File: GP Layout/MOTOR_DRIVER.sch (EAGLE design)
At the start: 34 parts, among them U2 CSD18502KCS_KCS_3, U3 MIC4604YM, U4 CSD18502KCS_KCS_3, U5 CSD18502KCS_KCS_3, U6 MIC4604YM, U7 ATMEGA328P_TQFP, Y1 16MHz

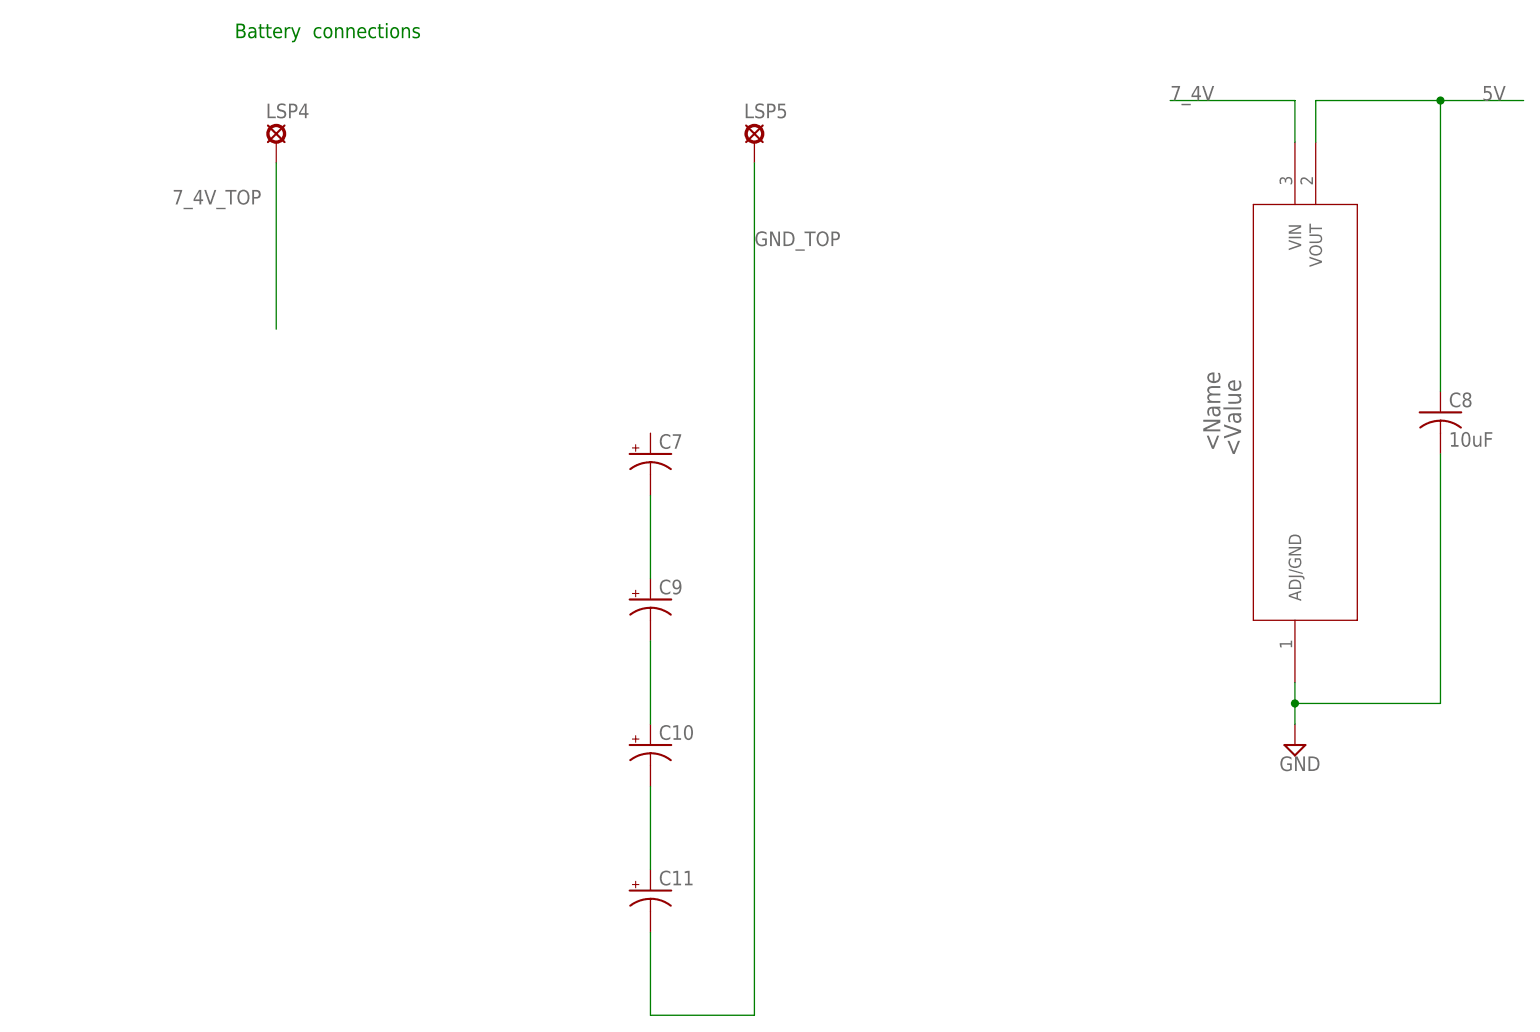
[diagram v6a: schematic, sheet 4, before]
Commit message: modified power schematic, added battery sense, named motor terminals
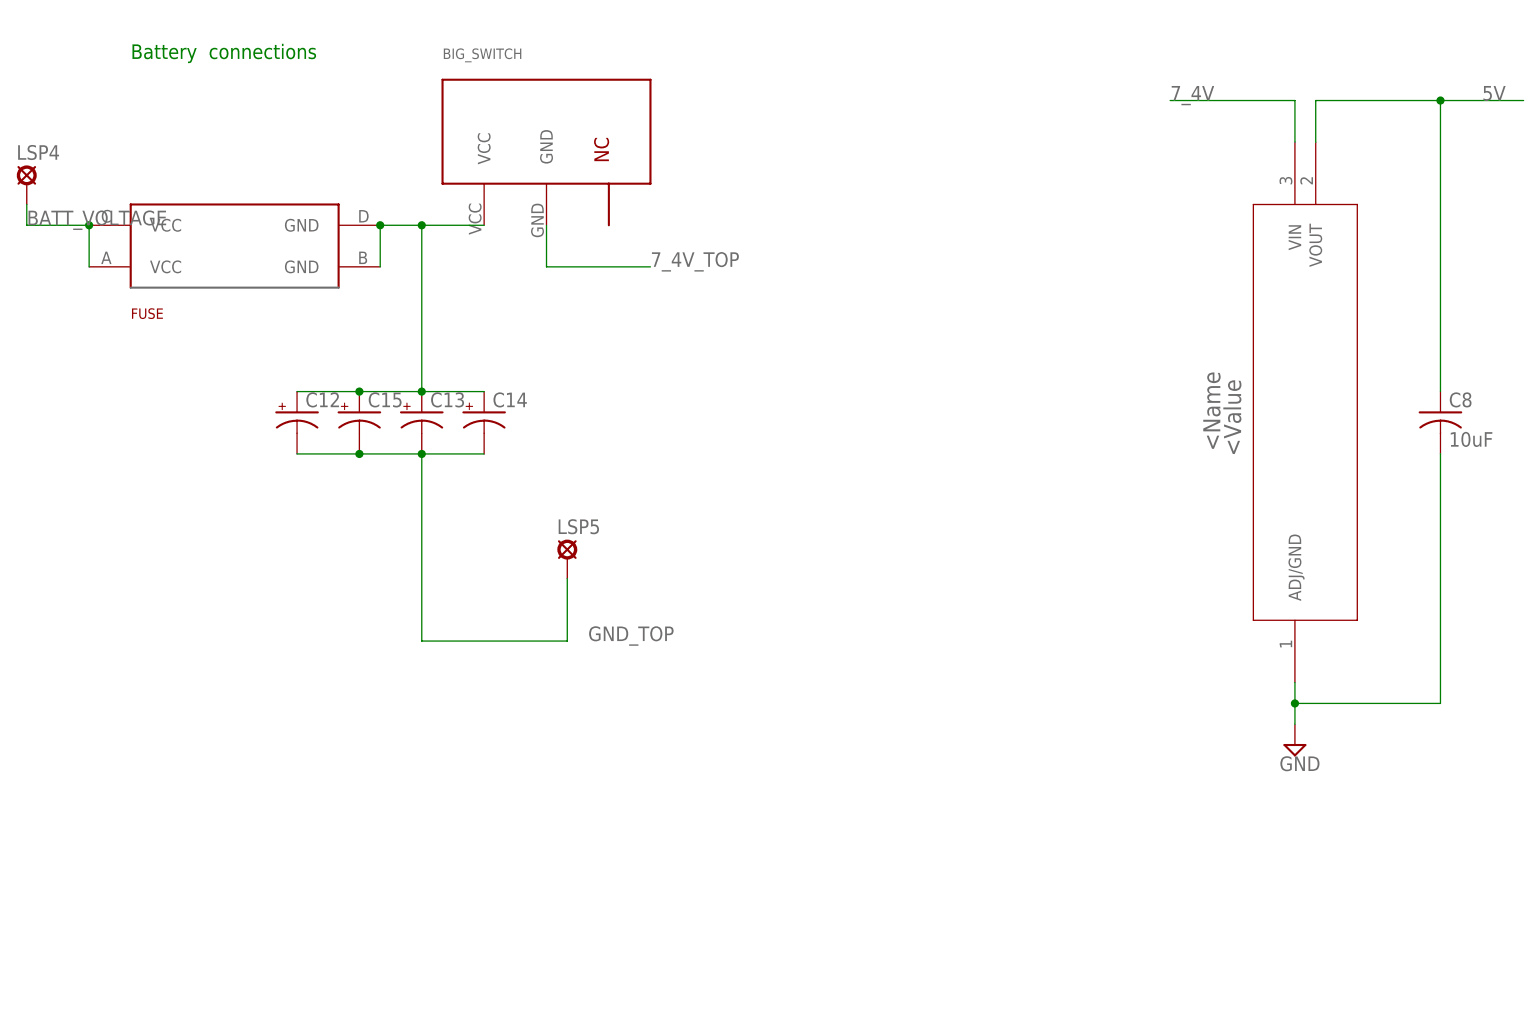
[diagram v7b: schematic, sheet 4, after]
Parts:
- removed C10, C11, C7, C9: (no value), resistor:CPOL-US153CLV-1010
- added BIG_SWITCH: (no value), bigswitch:BIGSWITCH
- added C12, C13, C14, C15: (no value), resistor:CPOL-US153CLV-1010
- added FUSE: (no value), minifuse:FUSEHOLDER3588
- added R1: 2.8M, SparkFun-Resistors:0.3OHM-0805-1/8W-1%
- added R2: 1.62M, SparkFun-Resistors:0.3OHM-0805-1/8W-1%
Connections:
- net N$1 renamed MOTOR_HIGH
- net N$8 renamed MOTOR_LOW
- removed net N$14: C10.-, C11.+
- removed net N$17: C10.+, C9.-
- removed net N$19: C7.-, C9.+
- new net BATT_VOLTAGE: FUSE.VCC@A, FUSE.VCC@C, LSP4.MP, R1.2
- new net BATT_VOLTAGE_SENSE: R1.1, R2.2, U$1.14/A0
- new net N$21: BIG_SWITCH.VCC, C12.+, C13.+, C14.+, C15.+, FUSE.GND@B, FUSE.GND@D
- net 7_4V_TOP: now also BIG_SWITCH.GND; no longer LSP4.MP
- net GND: now also R2.1
- net GND_TOP: now also C12.-, C13.-, C14.-, C15.-; no longer C11.-
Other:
- moved on the sheet: LSP4, LSP5
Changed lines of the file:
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@@
 <?xml version="1.0" encoding="utf-8"?>
 <!DOCTYPE eagle SYSTEM "eagle.dtd">
-<eagle version="8.0.0">
+<eagle version="8.0.1">
 <drawing>
 <settings>
@@
 <part name="SUPPLY1" library="supply2" deviceset="GND" device=""/>
 <part name="C8" library="resistor" deviceset="C-US" device="050-025X075" value="10uF"/>
-<part name="C7" library="resistor" deviceset="CPOL-US" device="153CLV-1010"/>
-<part name="C9" library="resistor" deviceset="CPOL-US" device="153CLV-1010"/>
-<part name="C10" library="resistor" deviceset="CPOL-US" device="153CLV-1010"/>
-<part name="C11" library="resistor" deviceset="CPOL-US" device="153CLV-1010"/>
+<part name="C12" library="resistor" deviceset="CPOL-US" device="153CLV-1010"/>
+<part name="C13" library="resistor" deviceset="CPOL-US" device="153CLV-1010"/>
+<part name="C14" library="resistor" deviceset="CPOL-US" device="153CLV-1010"/>
+<part name="C15" library="resistor" deviceset="CPOL-US" device="153CLV-1010"/>
+<part name="FUSE" library="minifuse" deviceset="FUSEHOLDER3588" device=""/>
+<part name="BIG_SWITCH" library="bigswitch" deviceset="BIGSWITCH" device=""/>
+<part name="R1" library="SparkFun-Resistors" deviceset="0.3OHM" device="-0805-1/8W-1%" value="2.8M"/>
+<part name="R2" library="SparkFun-Resistors" deviceset="0.3OHM" device="-0805-1/8W-1%" value="1.62M"/>
+<part name="SUPPLY2" library="supply2" deviceset="GND" device=""/>
 </parts>
 <sheets>
@@
 </busses>
 <nets>
-<net name="N$1" class="0">
+<net name="MOTOR_HIGH" class="0">
 <segment>
 <pinref part="TOP_FWD" gate="A" pin="SOURCE"/>
@@
 <wire x1="139.7" y1="132.08" x2="127" y2="132.08" width="0.1524" layer="91"/>
 <junction x="127" y="132.08"/>
+<label x="127" y="134.62" size="1.778" layer="95"/>
 </segment>
 </net>
@@
 </segment>
 </net>
-<net name="N$8" class="0">
+<net name="MOTOR_LOW" class="0">
 <segment>
 <pinref part="U4" gate="A" pin="SOURCE"/>
@@
 <wire x1="228.6" y1="132.08" x2="241.3" y2="132.08" width="0.1524" layer="91"/>
 <junction x="241.3" y="132.08"/>
+<label x="228.6" y="134.62" size="1.778" layer="95"/>
 </segment>
 </net>
@@
 <instance part="SUPPLY5" gate="GND" x="320.04" y="154.94"/>
 <instance part="SUPPLY6" gate="GND" x="317.5" y="121.92"/>
+<instance part="R1" gate="G$1" x="342.9" y="144.78" rot="R90"/>
+<instance part="R2" gate="G$1" x="342.9" y="129.54" rot="R90"/>
+<instance part="SUPPLY2" gate="GND" x="342.9" y="119.38"/>
 </instances>
 <busses>
@@
 <pinref part="SUPPLY6" gate="GND" pin="GND"/>
 </segment>
+<segment>
+<pinref part="R2" gate="G$1" pin="1"/>
+<pinref part="SUPPLY2" gate="GND" pin="GND"/>
+<wire x1="342.9" y1="124.46" x2="342.9" y2="121.92" width="0.1524" layer="91"/>
+</segment>
 </net>
 <net name="N$6" class="0">
@@
 <wire x1="289.56" y1="167.64" x2="279.4" y2="167.64" width="0.1524" layer="91"/>
 <label x="284.48" y="167.64" size="1.778" layer="95"/>
+</segment>
+</net>
+<net name="BATT_VOLTAGE_SENSE" class="0">
+<segment>
+<pinref part="U$1" gate="G$1" pin="14/A0"/>
+<wire x1="279.4" y1="137.16" x2="342.9" y2="137.16" width="0.1524" layer="91"/>
+<pinref part="R1" gate="G$1" pin="1"/>
+<wire x1="342.9" y1="137.16" x2="342.9" y2="139.7" width="0.1524" layer="91"/>
+<pinref part="R2" gate="G$1" pin="2"/>
+<wire x1="342.9" y1="134.62" x2="342.9" y2="137.16" width="0.1524" layer="91"/>
+<junction x="342.9" y="137.16"/>
+<label x="312.42" y="137.16" size="1.778" layer="95"/>
+</segment>
+</net>
+<net name="BATT_VOLTAGE" class="0">
+<segment>
+<pinref part="R1" gate="G$1" pin="2"/>
+<wire x1="342.9" y1="149.86" x2="342.9" y2="157.48" width="0.1524" layer="91"/>
+<label x="342.9" y="157.48" size="1.778" layer="95"/>
 </segment>
 </net>
@@
 <description>Power Schematic</description>
 <plain>
-<text x="38.1" y="243.84" size="1.778" layer="91">Battery  connections</text>
+<text x="25.4" y="241.3" size="1.778" layer="91">Battery  connections</text>
 </plain>
 <instances>
 <instance part="FRAME4" gate="G$1" x="0" y="0"/>
-<instance part="LSP4" gate="1" x="43.18" y="231.14"/>
-<instance part="LSP5" gate="1" x="101.6" y="231.14"/>
+<instance part="LSP4" gate="1" x="12.7" y="226.06"/>
+<instance part="LSP5" gate="1" x="78.74" y="180.34"/>
 <instance part="U$3" gate="A" x="167.64" y="165.1" rot="R90"/>
 <instance part="SUPPLY1" gate="GND" x="167.64" y="157.48"/>
 <instance part="C8" gate="G$1" x="185.42" y="198.12"/>
-<instance part="C7" gate="G$1" x="88.9" y="193.04"/>
-<instance part="C9" gate="G$1" x="88.9" y="175.26"/>
-<instance part="C10" gate="G$1" x="88.9" y="157.48"/>
-<instance part="C11" gate="G$1" x="88.9" y="139.7"/>
+<instance part="C12" gate="G$1" x="45.72" y="198.12"/>
+<instance part="C13" gate="G$1" x="60.96" y="198.12"/>
+<instance part="C14" gate="G$1" x="68.58" y="198.12"/>
+<instance part="C15" gate="G$1" x="53.34" y="198.12"/>
+<instance part="FUSE" gate="G$1" x="38.1" y="218.44" rot="MR180"/>
+<instance part="BIG_SWITCH" gate="G$1" x="68.58" y="226.06"/>
 </instances>
 <busses>
@@
 </segment>
 </net>
-<net name="7_4V_TOP" class="0">
-<segment>
-<pinref part="LSP4" gate="1" pin="MP"/>
-<wire x1="43.18" y1="228.6" x2="43.18" y2="208.28" width="0.1524" layer="91"/>
-<label x="30.48" y="223.52" size="1.778" layer="95"/>
-</segment>
-</net>
 <net name="GND_TOP" class="0">
 <segment>
+<pinref part="C12" gate="G$1" pin="-"/>
+<pinref part="C15" gate="G$1" pin="-"/>
+<wire x1="45.72" y1="193.04" x2="53.34" y2="193.04" width="0.1524" layer="91"/>
+<pinref part="C13" gate="G$1" pin="-"/>
+<wire x1="53.34" y1="193.04" x2="60.96" y2="193.04" width="0.1524" layer="91"/>
+<junction x="53.34" y="193.04"/>
+<pinref part="C14" gate="G$1" pin="-"/>
+<wire x1="60.96" y1="193.04" x2="68.58" y2="193.04" width="0.1524" layer="91"/>
+<junction x="60.96" y="193.04"/>
+<label x="81.28" y="170.18" size="1.778" layer="95"/>
 <pinref part="LSP5" gate="1" pin="MP"/>
-<label x="101.6" y="218.44" size="1.778" layer="95"/>
-<wire x1="101.6" y1="228.6" x2="101.6" y2="124.46" width="0.1524" layer="91"/>
-<pinref part="C11" gate="G$1" pin="-"/>
-<wire x1="101.6" y1="124.46" x2="88.9" y2="124.46" width="0.1524" layer="91"/>
-<wire x1="88.9" y1="124.46" x2="88.9" y2="134.62" width="0.1524" layer="91"/>
+<wire x1="78.74" y1="177.8" x2="78.74" y2="170.18" width="0.1524" layer="91"/>
+<wire x1="78.74" y1="170.18" x2="60.96" y2="170.18" width="0.1524" layer="91"/>
+<wire x1="60.96" y1="170.18" x2="60.96" y2="193.04" width="0.1524" layer="91"/>
 </segment>
 </net>
@@
 </segment>
 </net>
-<net name="N$14" class="0">
-<segment>
-<pinref part="C11" gate="G$1" pin="+"/>
-<pinref part="C10" gate="G$1" pin="-"/>
-<wire x1="88.9" y1="142.24" x2="88.9" y2="152.4" width="0.1524" layer="91"/>
-</segment>
-</net>
-<net name="N$17" class="0">
-<segment>
-<pinref part="C10" gate="G$1" pin="+"/>
-<pinref part="C9" gate="G$1" pin="-"/>
-<wire x1="88.9" y1="160.02" x2="88.9" y2="170.18" width="0.1524" layer="91"/>
-</segment>
-</net>
-<net name="N$19" class="0">
-<segment>
-<pinref part="C9" gate="G$1" pin="+"/>
-<pinref part="C7" gate="G$1" pin="-"/>
-<wire x1="88.9" y1="177.8" x2="88.9" y2="187.96" width="0.1524" layer="91"/>
-</segment>
-</net>
+<net name="7_4V_TOP" class="0">
+<segment>
+<pinref part="BIG_SWITCH" gate="G$1" pin="GND"/>
+<wire x1="76.2" y1="220.98" x2="76.2" y2="215.9" width="0.1524" layer="91"/>
+<wire x1="76.2" y1="215.9" x2="88.9" y2="215.9" width="0.1524" layer="91"/>
+<label x="88.9" y="215.9" size="1.778" layer="95"/>
+</segment>
+</net>
+<net name="BATT_VOLTAGE" class="0">
+<segment>
+<pinref part="LSP4" gate="1" pin="MP"/>
+<wire x1="12.7" y1="223.52" x2="12.7" y2="220.98" width="0.1524" layer="91"/>
+<wire x1="12.7" y1="220.98" x2="20.32" y2="220.98" width="0.1524" layer="91"/>
+<pinref part="FUSE" gate="G$1" pin="VCC@C"/>
+<pinref part="FUSE" gate="G$1" pin="VCC@A"/>
+<wire x1="20.32" y1="220.98" x2="20.32" y2="215.9" width="0.1524" layer="91"/>
+<junction x="20.32" y="220.98"/>
+<label x="12.7" y="220.98" size="1.778" layer="95"/>
+</segment>
+</net>
+<net name="N$21" class="0">
+<segment>
+<pinref part="FUSE" gate="G$1" pin="GND@D"/>
+<pinref part="FUSE" gate="G$1" pin="GND@B"/>
+<wire x1="55.88" y1="220.98" x2="55.88" y2="215.9" width="0.1524" layer="91"/>
+<pinref part="BIG_SWITCH" gate="G$1" pin="VCC"/>
+<wire x1="55.88" y1="220.98" x2="60.96" y2="220.98" width="0.1524" layer="91"/>
+<junction x="55.88" y="220.98"/>
+<pinref part="C12" gate="G$1" pin="+"/>
+<pinref part="C15" gate="G$1" pin="+"/>
+<wire x1="60.96" y1="220.98" x2="68.58" y2="220.98" width="0.1524" layer="91"/>
+<wire x1="45.72" y1="200.66" x2="53.34" y2="200.66" width="0.1524" layer="91"/>
+<pinref part="C13" gate="G$1" pin="+"/>
+<wire x1="53.34" y1="200.66" x2="60.96" y2="200.66" width="0.1524" layer="91"/>
+<junction x="53.34" y="200.66"/>
+<pinref part="C14" gate="G$1" pin="+"/>
+<wire x1="60.96" y1="200.66" x2="68.58" y2="200.66" width="0.1524" layer="91"/>
+<junction x="60.96" y="200.66"/>
+<wire x1="60.96" y1="220.98" x2="60.96" y2="200.66" width="0.1524" layer="91"/>
+<junction x="60.96" y="220.98"/>
+</segment>
+</net>

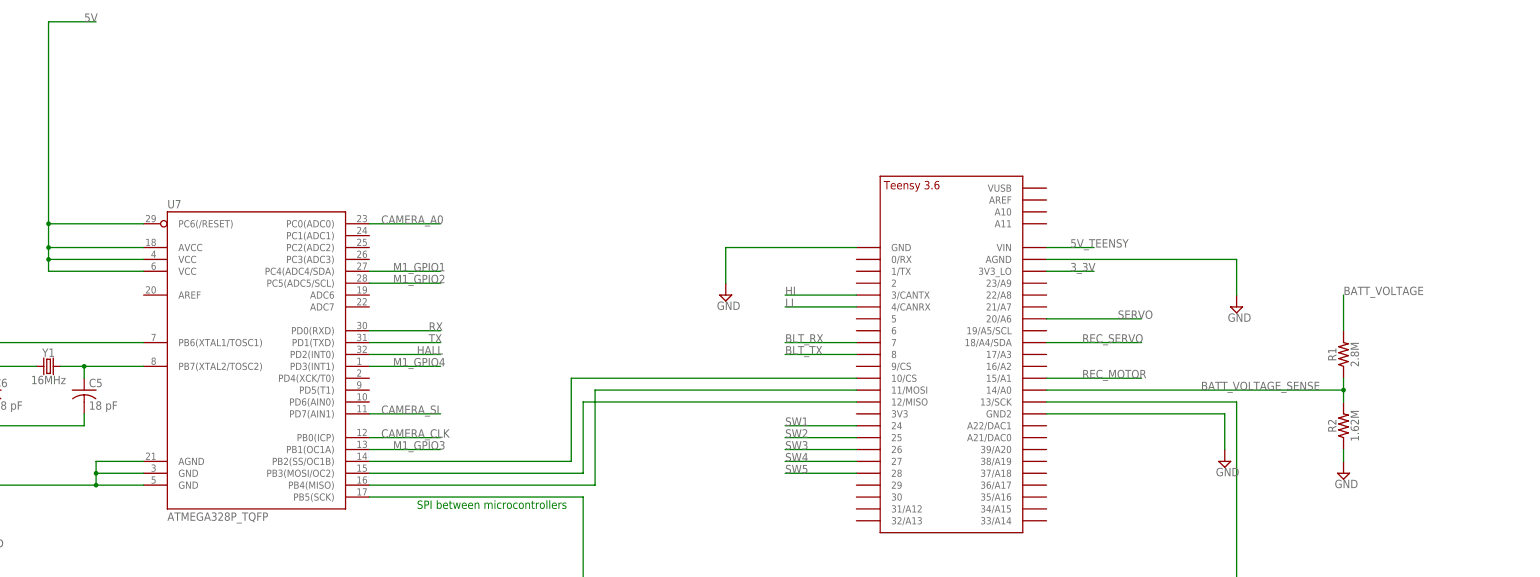
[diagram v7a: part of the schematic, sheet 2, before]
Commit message: added some heatsink outlines
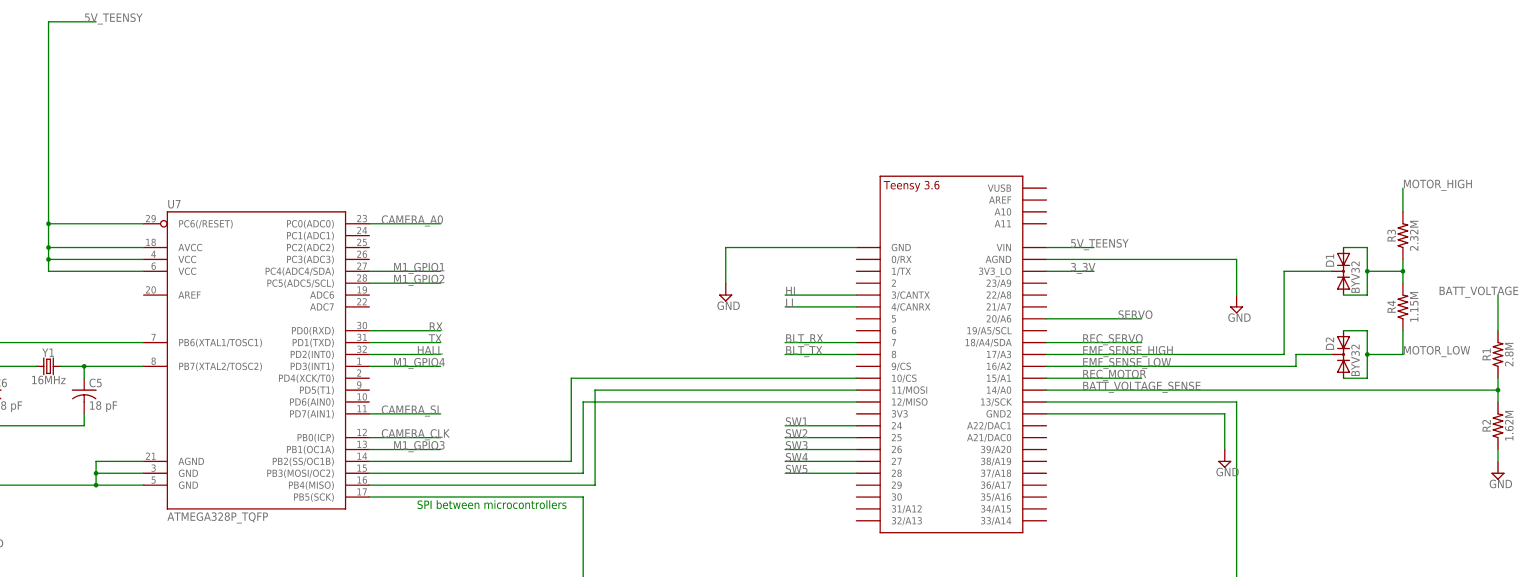
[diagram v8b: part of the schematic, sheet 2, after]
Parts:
- added D1, D2: BYV32, diode:BYV32
- added R3: 2.32M, SparkFun-Resistors:0.3OHM-0805-1/8W-1%
- added R4: 1.15M, SparkFun-Resistors:0.3OHM-0805-1/8W-1%
- added U$2, U$4, U$5, U$6: HEATSINK, heatsink:HEATSINK
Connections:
- new net EMF_SENSE_HIGH: D1.C, U$1.17/A3
- new net EMF_SENSE_LOW: D2.C, U$1.16/A2
- new net MOTOR_HIGH_TOP: LSP3.MP, SV6.3, TOP_FWD.SOURCE, U2.DRAIN
- new net MOTOR_LOW_TOP: LSP6.MP, SV6.4, U4.SOURCE, U5.DRAIN
- new net N$1: D1.A1, D1.A2, R3.1, R4.2
- net 5V: no longer U7.AVCC, U7.PC6(/RESET), U7.VCC@4, U7.VCC@6
- net 5V_TEENSY: now also U7.AVCC, U7.PC6(/RESET), U7.VCC@4, U7.VCC@6
- net MOTOR_HIGH: now also R3.2, SV2.3; no longer LSP3.MP, TOP_FWD.SOURCE, U2.DRAIN
- net MOTOR_LOW: now also D2.A1, D2.A2, R4.1, SV2.4; no longer LSP6.MP, U4.SOURCE, U5.DRAIN
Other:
- moved on the sheet: R1, R2, TOP_FWD
